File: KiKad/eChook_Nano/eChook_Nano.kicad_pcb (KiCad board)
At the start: 2 copper layers, 75 x 75 mm, 53 parts, among them J1 Expansion, Q1 BC547, U1 Arduino_Nano_v3.x, U2 TSR_1-2450, U3 MCP6002-xP

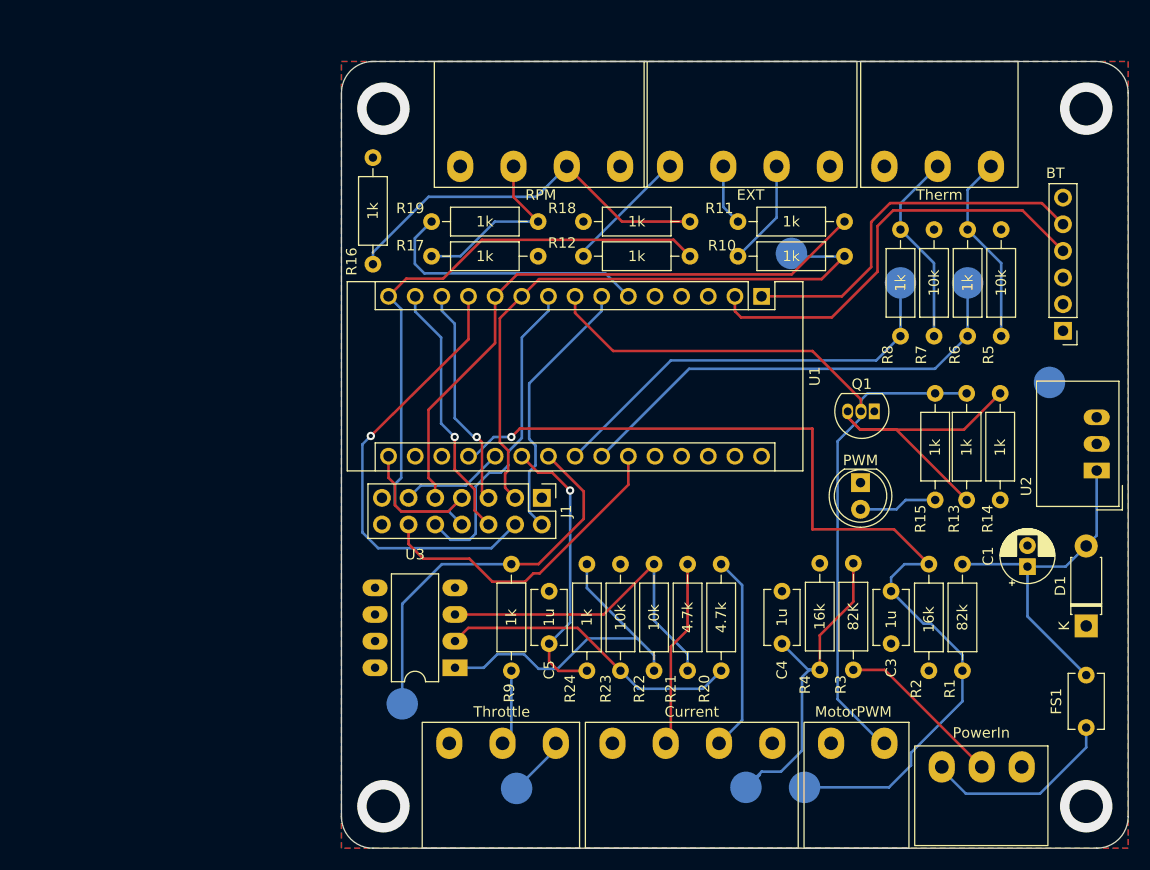
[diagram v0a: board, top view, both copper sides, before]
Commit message: Added 3D models and layout/silkscreen improvements
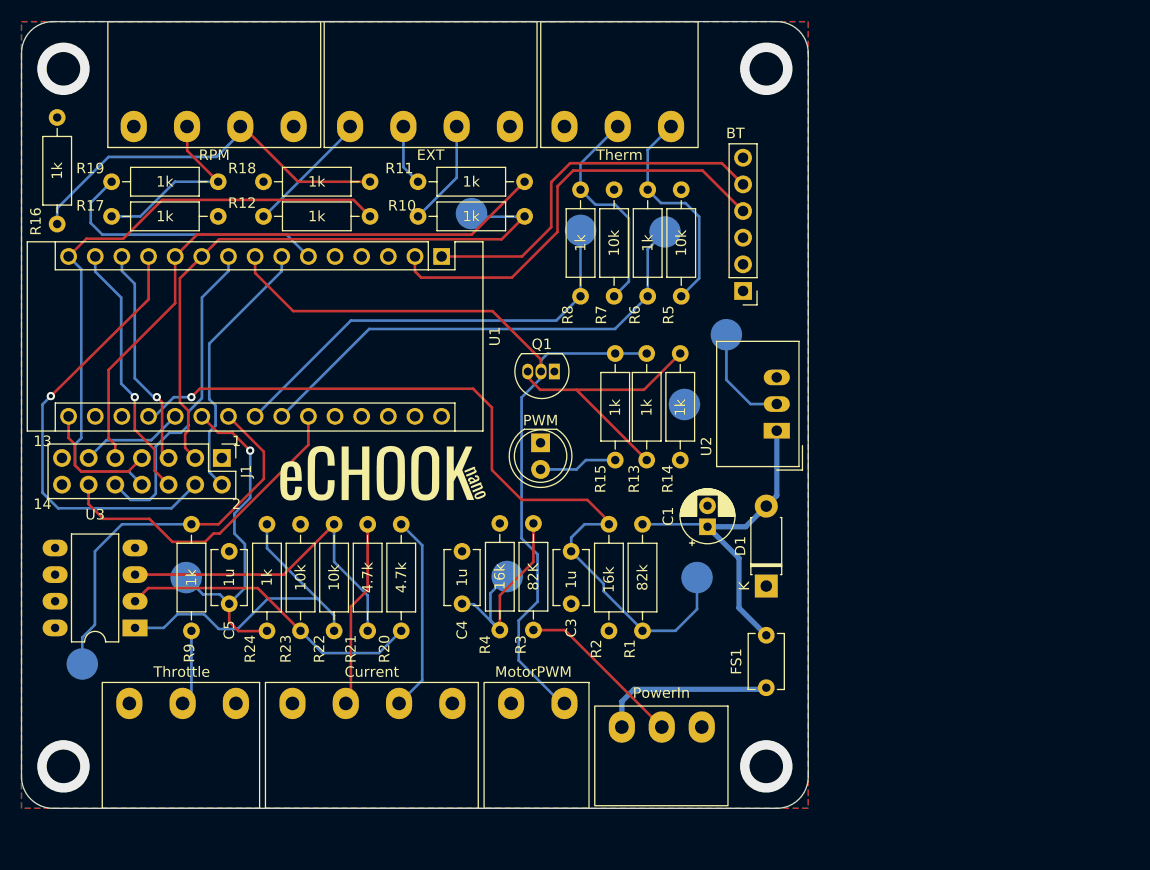
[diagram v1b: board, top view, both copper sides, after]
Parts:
- added G***: LOGO, user:eCHOOK_NANO_Logo_20mm, F.Cu at (144.0, 104.2)
- added TP9: CurrentTP, TestPoint:TestPoint_Pad_D3.0mm, B.Cu at (125.2, 114.2)
- moved TP4 47.7 mm to (176.7, 91.0)
- moved TP3 34.9 mm to (172.7, 97.7)
- moved Conn4 31.4 mm to (135.4, 71.2)
- moved TP6 30.9 mm to (162.8, 81.1)
- moved Conn2 30.7 mm to (166.7, 128.4)
- moved Conn8 30.7 mm to (158.3, 130.2)
- moved G*** 30.7 mm to (133.0, 91.1)
- moved C1 30.7 mm to (174.9, 109.4)
- moved C3 30.7 mm to (161.9, 111.7)
- moved C4 30.7 mm to (151.5, 116.7)
- moved C5 30.7 mm to (129.3, 116.7)
- moved Conn1 30.7 mm to (135.3, 126.2)
- moved Conn3 30.7 mm to (171.4, 71.2)
- moved Conn5 30.7 mm to (156.1, 71.2)
- moved Conn6 30.7 mm to (119.8, 126.2)
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- renumbered Conn to Conn1
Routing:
- net /BattTotalV: track 94.8 -> 78.2 mm
- net /Batt1v: track 33.7 -> 22.4 mm
- net Net-(Q1-Pad3): track 32.2 -> 25.9 mm
- net /CurrentSens: track 27.1 -> 33.0 mm
- net GND: track 5.85 -> 10.1 mm
- net Net-(Conn3-Pad1): track 18.4 -> 21.2 mm
- net Net-(Conn3-Pad2): track 19.0 -> 21.2 mm
- net /Temp1: track 44.7 -> 46.4 mm
- net Net-(Conn2-Pad1): track 18.7 -> 17.0 mm
- net Net-(Conn6-Pad2): track 7.27 -> 6.08 mm
- net Net-(Conn1-Pad2): track 17.9 -> 17.3 mm
- net /WheelRPM: track 26.3 -> 26.8 mm
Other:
- board text added: "+12V"
- board text added: "1"
- board text added: "13"
- board text added: "14"
- board text added: "2"
- board text added: "2022 v1.3.1"
- board text added: "3"
- board text added: "4"
- board text added: "Brake In"
- board text added: "Buttons"
- board text added: "Current"
- board text added: "Documentation at docs.echook.uk"
- board text added: "Motor RPM"
- board text added: "MotorPWM"
- board text added: "PWM"
- board text added: "PowerIn"
- board text added: "RPM"
- board text added: "Race Start"
- board text added: "Ref"
- board text added: "Sense"
- board text added: "Switch Screen"
- board text added: "Thermistors"
- board text added: "Throttle"
- board text added: "Thrtl"
- board text added: "Tmp1"
- board text added: "Tmp2"
- board text added: "Wheel RPM"
- board text removed: "Documentation @ docs.echook.uk"
- board text removed: "eCHOOKnano v1.3.1"

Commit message: Updated ext. pin out
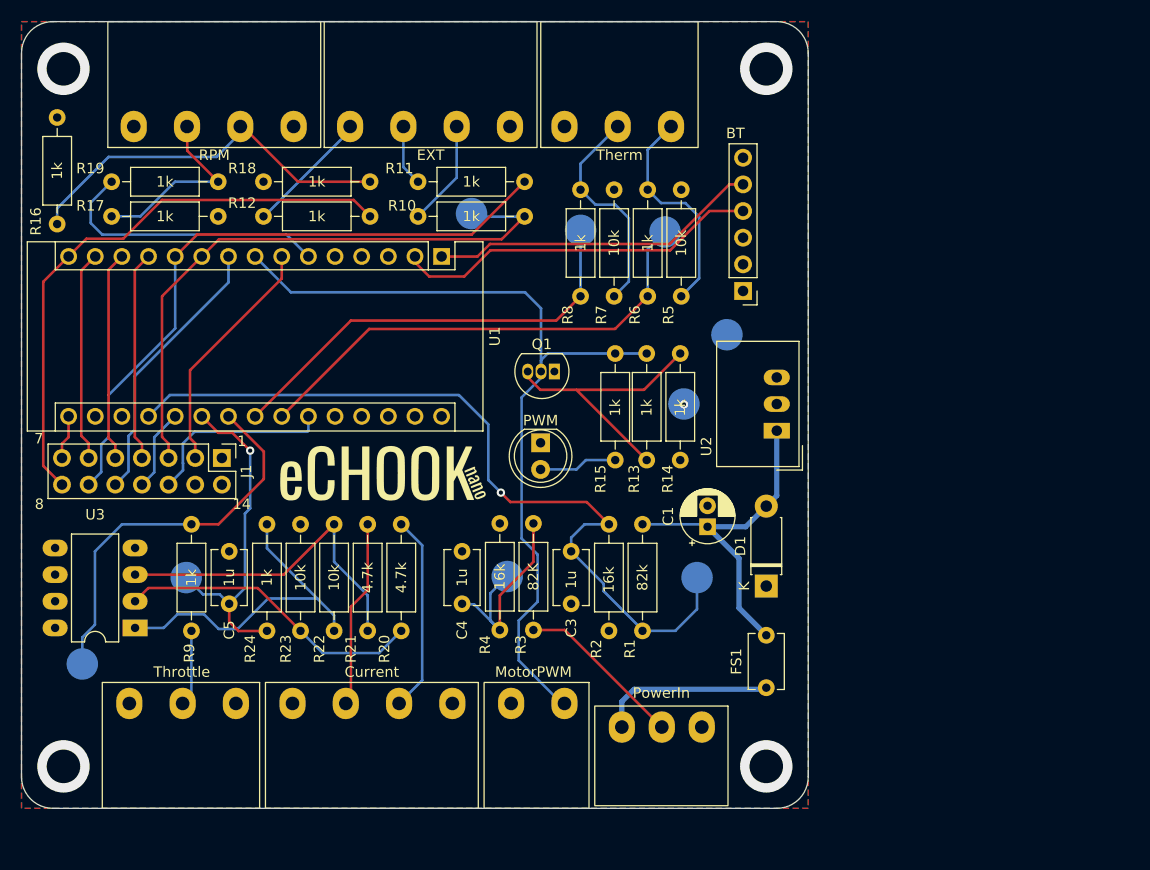
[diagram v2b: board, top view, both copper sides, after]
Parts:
- moved TP3 7.79 mm to (176.8, 91.0)
- moved TP4 7.74 mm to (172.7, 97.7)
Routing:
- net /D9: track 42.8 -> 20.0 mm, vias 1 -> 0
- net /A6: track 30.9 -> 18.3 mm
- net GND: track 10.1 -> 0.00 mm, vias 0 -> 1
- net /D13: track 12.1 -> 4.23 mm
- net /BT_In: track 41.3 -> 35.0 mm
- net /D6: track 30.8 -> 26.2 mm
- net /D11: track 24.6 -> 20.1 mm, vias 1 -> 0
- net /DriverButton2: track 59.4 -> 55.1 mm
- net /BT_Out: track 35.8 -> 31.6 mm
- net /DriverButton: track 58.4 -> 61.4 mm
- net /D4: track 25.6 -> 23.0 mm
- net /A1: track 9.89 -> 7.82 mm
- net /MotorPWM: track 79.7 -> 81.6 mm
- net /D10: track 21.2 -> 20.0 mm, vias 1 -> 0
- net /CurrentSens: track 33.0 -> 32.2 mm
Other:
- board text added: "7"
- board text added: "8"
- board text added: "GNDTP"
- board text removed: "13"
